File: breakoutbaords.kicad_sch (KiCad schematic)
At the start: 14 parts, among them J13 USB_A, J15 Conn_01x16, J16 Conn_01x16, J3 Conn_01x12, J4 Conn_01x12, J5 USB_C_Receptacle_USB2.0_16P, U3 AMS1117-3.3

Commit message: added lcsc_id
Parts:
- J5: lcsd_id (none) -> C2686963
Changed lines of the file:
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@@
+			)
+		)
+		(property "lcsd_id" "C2686963"
+			(at 144.78 78.74 0)
+			(effects
+				(font
+					(size 1.27 1.27)
+				)
+				(hide yes)
 			)
 		)

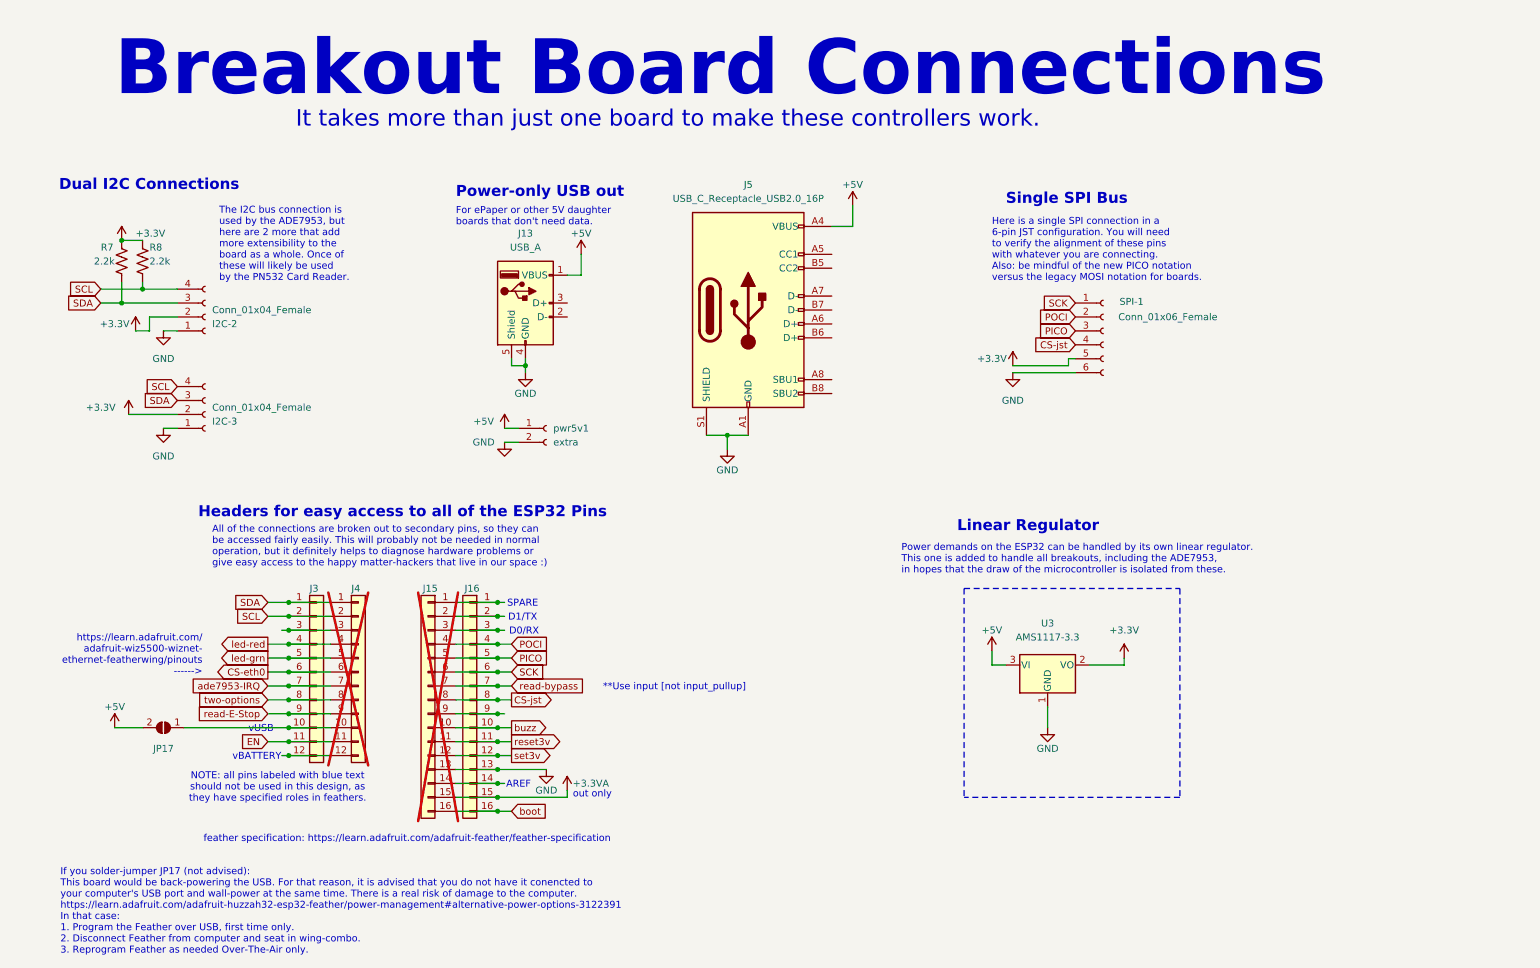
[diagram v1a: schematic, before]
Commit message: moved LED GPIO to fit free pins for ethernet wing
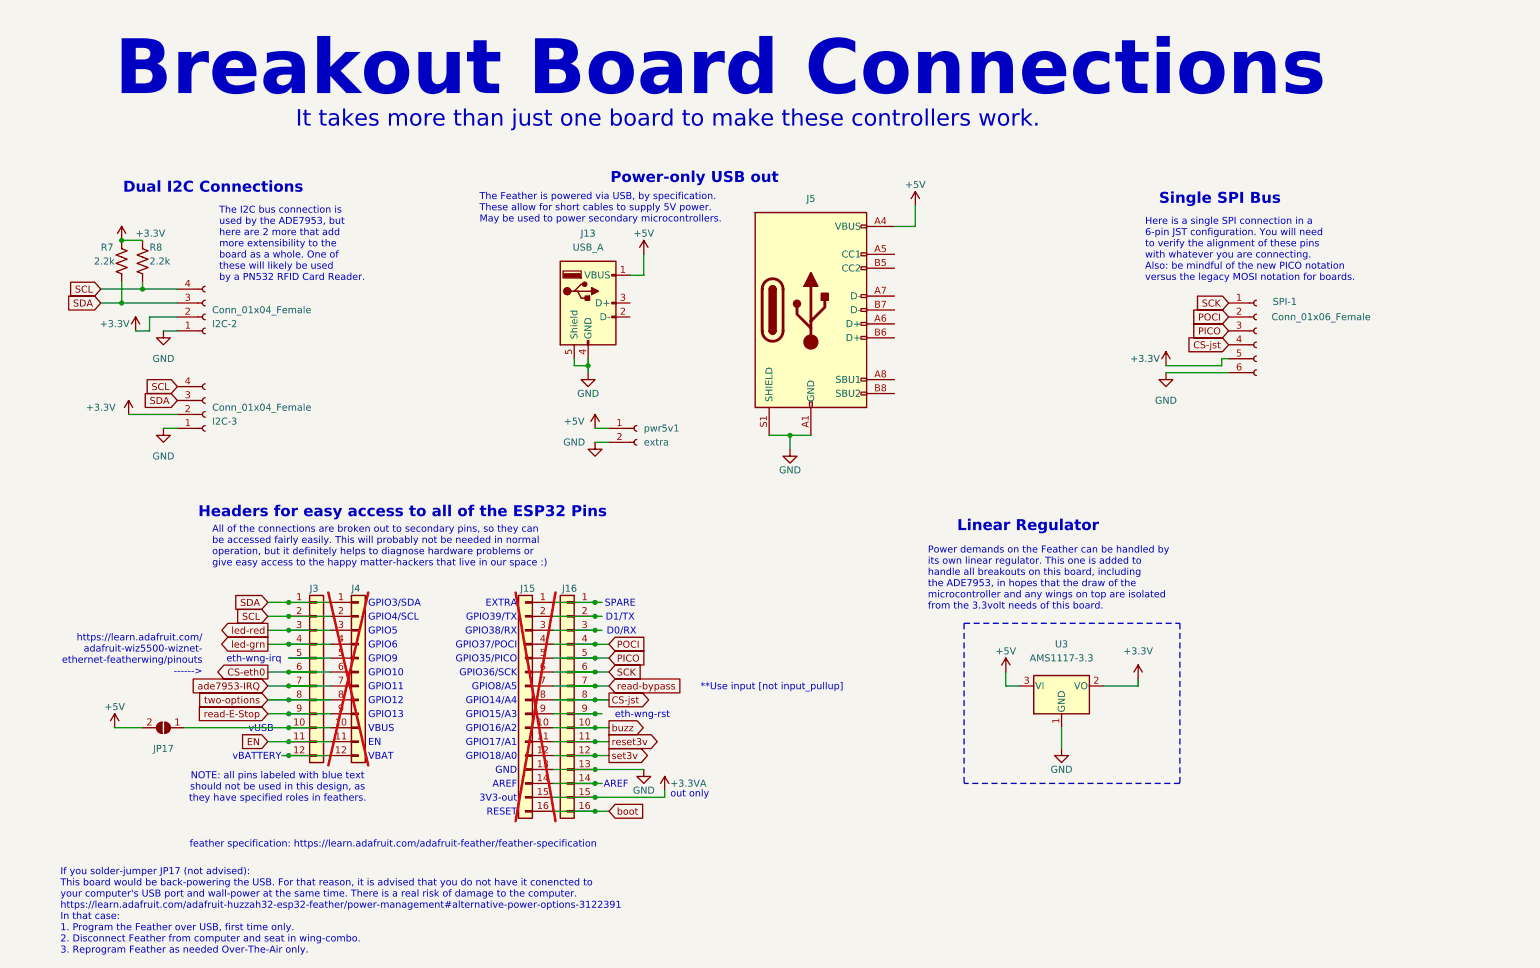
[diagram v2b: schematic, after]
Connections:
- net led-grn: now also J3.4 (Pin_4), J4.4 (Pin_4); no longer J3.5 (Pin_5), J4.5 (Pin_5)
- net led-red: now also J3.3 (Pin_3), J4.3 (Pin_3); no longer J3.4 (Pin_4), J4.4 (Pin_4)
- new net: J3.5 (Pin_5), J4.5 (Pin_5)
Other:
- note added: "3V3-out"
- note added: "EN"
- note added: "EXTRA"
- note added: "GND"
- note added: "GPIO10"
- note added: "GPIO11"
- note added: "GPIO12"
- note added: "GPIO13"
- note added: "GPIO14/A4"
- note added: "GPIO15/A3"
- note added: "GPIO16/A2"
- note added: "GPIO17/A1"
- note added: "GPIO18/A0"
- note added: "GPIO3/SDA"
- note added: "GPIO35/PICO"
- note added: "GPIO36/SCK"
- note added: "GPIO37/POCI"
- note added: "GPIO38/RX"
- note added: "GPIO39/TX"
- note added: "GPIO4/SCL"
- note added: "GPIO5"
- note added: "GPIO6"
- note added: "GPIO8/A5"
- note added: "GPIO9"
- note added: "Power demands on the Feather can be handled by its own linear regulator. This one is added to handle all breakouts on this board, including the ADE7953, in hopes that the draw of the microcontroller and any wings on top are isolated from the 3.3volt needs of this board."
- note added: "RESET"
- note added: "The Feather is powered via USB, by specification. These allow for short cables to supply 5V power. May be used to power secondary microcontrollers."
- note added: "The I2C bus connection is used by the ADE7953, but here are 2 more that add more extensibility to the board as a whole. One of these will likely be used by a PN532 RFID Card Reader."
- note added: "VBAT"
- note added: "VBUS"
- note added: "eth-wng-irq"
- note added: "eth-wng-rst"
- note removed: "For ePaper or other 5V daughter boards that don't need data."
- note removed: "Power demands on the ESP32 can be handled by its own linear regulator. This one is added to handle all breakouts, including the ADE7953, in hopes that the draw of the microcontroller is isolated from these."
- note removed: "The I2C bus connection is used by the ADE7953, but here are 2 more that add more extensibility to the board as a whole. Once of these will likely be used by the PN532 Card Reader."
- moved on the sheet: J13, J15, J16, J5, SPI-1, U3, pwr5v1

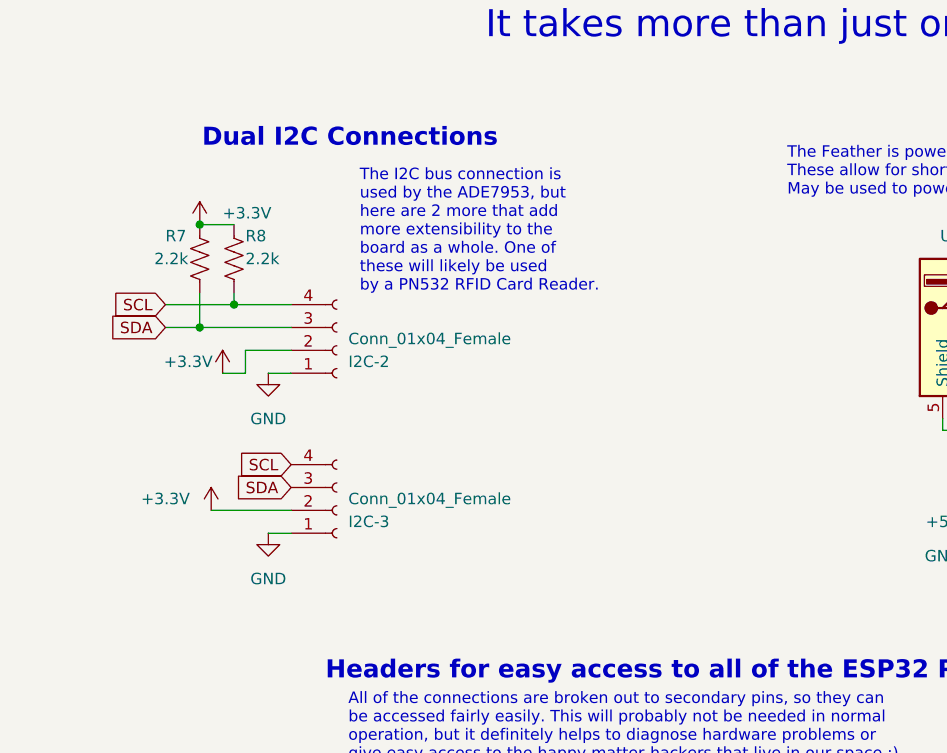
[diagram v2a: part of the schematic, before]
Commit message: working through DRC checks
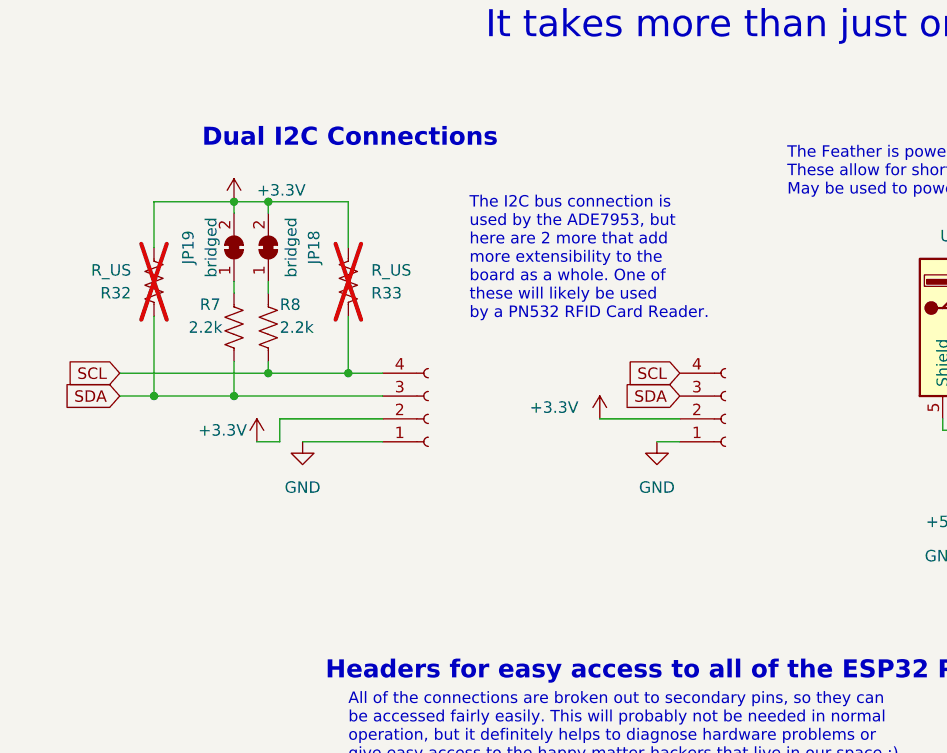
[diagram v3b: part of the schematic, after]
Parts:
- added JP18, JP19: bridged, Jumper:SolderJumper-2_P1.3mm_Bridged_RoundedPad1.0x1.5mm, symbol Jumper:SolderJumper_2_Bridged
- added R32, R33: R_US, Resistor_THT:R_Axial_DIN0204_L3.6mm_D1.6mm_P5.08mm_Horizontal, symbol Device:R_US
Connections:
- net +3.3V: now also JP18.2 (B), JP19.2 (B), R32.1, R33.1; no longer R7.2, R8.2
- net SCL: now also R33.2
- net SDA: now also R32.2
- new net: JP18.1 (A), R8.2
- new net: JP19.1 (A), R7.2
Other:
- moved on the sheet: R7, R8

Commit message: ordered B1P3 test run from JLCPCB
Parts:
- J16: JLCPCB Part # (none) -> C2905421
- J3: JLCPCB Part # (none) -> C2905419
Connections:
- net +3.3V: now also R7.2, R8.2; no longer JP18.2 (B), JP19.2 (B)
- net SCL: now also JP18.1 (A); no longer R8.1
- net SDA: now also JP19.1 (A); no longer R7.1
- new net: JP18.2 (B), R8.1
- new net: JP19.2 (B), R7.1
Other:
- note added: "The Feather is powered via USB, by specification. These allow for short cables to supply 5V power. May be also used to power secondary microcontrollers (like for e-Ink)."
- note removed: "The Feather is powered via USB, by specification. These allow for short cables to supply 5V power. May be used to power secondary microcontrollers."
- moved on the sheet: J13, J5, JP18, JP19, R7, R8, pwr5v1

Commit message: cleanup
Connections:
- net binary-current: now reaches J15.9 (Pin_9), J16.9 (Pin_9)
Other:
- note added: "eth-wng-rst **if not using binary current"
- note removed: "eth-wng-rst"
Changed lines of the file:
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@@
 	(wire
 		(pts
-			(xy 116.84 152.4) (xy 118.11 152.4)
+			(xy 116.84 152.4) (xy 119.38 152.4)
 		)
 		(stroke
@@
 		)
 	)
-	(text "eth-wng-rst"
-		(exclude_from_sim no)
-		(at 125.476 152.654 0)
-		(effects
-			(font
-				(size 1.27 1.27)
-			)
+	(text "eth-wng-rst\n  **if not using binary current"
+		(exclude_from_sim no)
+		(at 136.398 153.924 0)
+		(effects
+			(font
+				(size 1.27 1.27)
+			)
+			(justify left)
 		)
 	)
@@
 				(hide yes)
 			)
+		)
+	)
+	(global_label "binary-current"
+		(shape input)
+		(at 119.38 152.4 0)
+		(fields_autoplaced yes)
+		(effects
+			(font
+				(size 1.27 1.27)
+			)
+			(justify left)
+		)
+		(property "Intersheetrefs" "${INTERSHEET_REFS}"
+			(at 136.5165 152.4 0)
+			(effects
+				(font
+					(size 1.27 1.27)
+				)
+				(justify left)
+				(hide yes)
+			)
